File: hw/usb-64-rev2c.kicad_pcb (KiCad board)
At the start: 4 copper layers, 69.2 x 46.5 mm, 64 parts, among them J1 USB_C_Receptacle_PowerOnly_6P, J100 Conn_01x03_Pin, J2 USB_C_Receptacle_USB2.0_14P, J3 USB_C_Receptacle_USB2.0_14P, J300 DE9_Receptacle, J301 DE9_Receptacle, SW1 SW_Push, SW2 SW_Push, U100 NCP1117-3.3_SOT223, U200 RP2040, U201 W25Q128JVSIQ, U300 74AHCT1G125, U301 74AHCT1G125, U302 74AHCT1G125, U303 74AHCT1G125, U304 74AHCT1G125, U305 74AHCT1G125, U306 74AHCT1G125, U307 74AHCT1G125, U308 74AHCT1G125, U309 74AHCT1G125, X100 ASE-12MHz

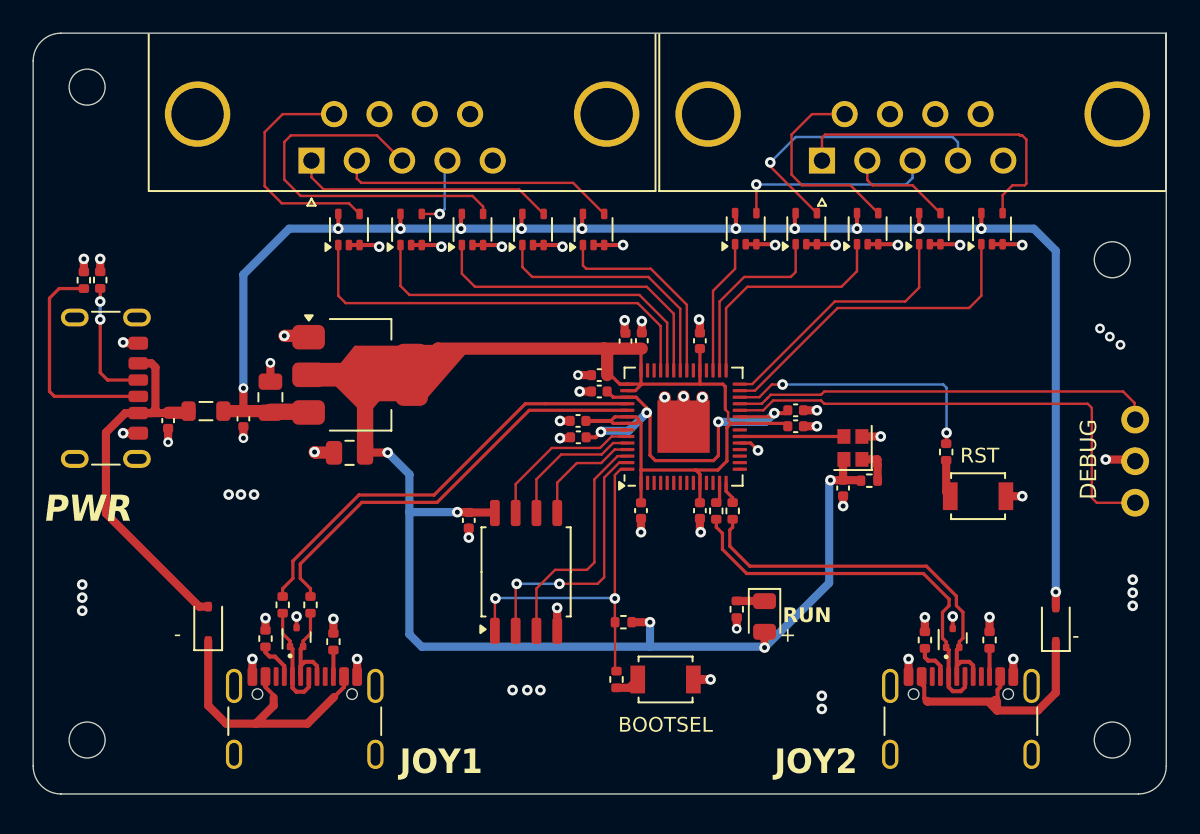
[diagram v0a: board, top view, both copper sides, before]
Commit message: changed pcb specs
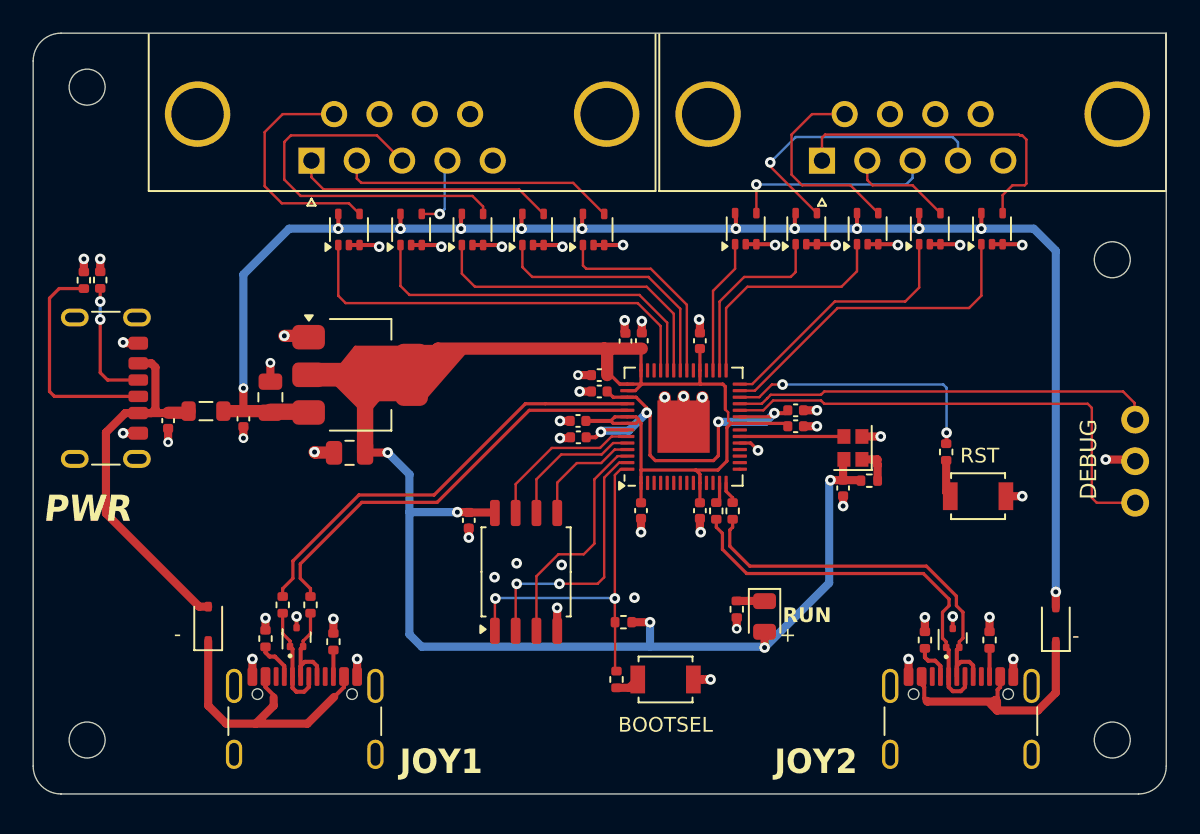
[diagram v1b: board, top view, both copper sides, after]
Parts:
- U100: value NCP1117-3.3_SOT223 -> NCP1117-3.3
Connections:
- J2 pad S1: GND -> unconnected-(J2-SHIELD-PadS1)_1
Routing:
- net GND: vias 69 -> 56
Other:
- board text added: "{ "ViaStitching": "0.2", "stitch_zone_0": { "HSpacing": "2", "VSpacing": "2", "Clearance": "0", "Randomize": false } }"
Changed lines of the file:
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@@
 		(56 "User.7" user)
 		(57 "User.8" user)
-		(58 "User.9" user)
+		(58 "User.9" user "plugins.config")
 	)
 	(setup
@@
 	(net 84 "/MCU/RUN")
 	(net 85 "Net-(R208-Pad2)")
+	(net 86 "unconnected-(J2-SHIELD-PadS1)")
+	(net 87 "unconnected-(J2-SHIELD-PadS1)_1")
+	(net 88 "unconnected-(J2-SHIELD-PadS1)_2")
+	(net 89 "unconnected-(J2-SHIELD-PadS1)_3")
 	(footprint "MountingHole:MountingHole_2.2mm_M2"
 		(layer "F.Cu")
@@
 			)
 		)
-		(property "Value" "NCP1117-3.3_SOT223"
+		(property "Value" "NCP1117-3.3"
 			(at 0 4.5 0)
 			(layer "F.Fab")
@@
 			(layers "*.Cu" "*.Mask" "F.Paste")
 			(remove_unused_layers no)
-			(net 2 "GND")
+			(net 86 "unconnected-(J2-SHIELD-PadS1)")
 			(pinfunction "SHIELD")
-			(pintype "passive")
+			(pintype "passive+no_connect")
 		)
 		(pad "S1" thru_hole oval
@@
 			(layers "*.Cu" "*.Mask" "F.Paste")
 			(remove_unused_layers no)
-			(net 2 "GND")
+			(net 88 "unconnected-(J2-SHIELD-PadS1)_2")
 			(pinfunction "SHIELD")
-			(pintype "passive")
+			(pintype "passive+no_connect")
 		)
 		(pad "S1" thru_hole oval
@@
 			(layers "*.Cu" "*.Mask" "F.Paste")
 			(remove_unused_layers no)
-			(net 2 "GND")
+			(net 89 "unconnected-(J2-SHIELD-PadS1)_3")
 			(pinfunction "SHIELD")
-			(pintype "passive")
+			(pintype "passive+no_connect")
 		)
 		(pad "S1" thru_hole oval
@@
 			(layers "*.Cu" "*.Mask" "F.Paste")
 			(remove_unused_layers no)
-			(net 2 "GND")
+			(net 87 "unconnected-(J2-SHIELD-PadS1)_1")
 			(pinfunction "SHIELD")
-			(pintype "passive")
+			(pintype "passive+no_connect")
 		)
 		(model "${KICAD8_3DMODEL_DIR}/Connector_USB.3dshapes/USB_C_Receptacle_GCT_USB4105-xx-A_16P_TopMnt_Horizontal.wrl"
@@
 		)
 	)
+	(gr_text "{\n  \"ViaStitching\": \"0.2\",\n  \"stitch_zone_0\": {\n    \"HSpacing\": \"2\",\n    \"VSpacing\": \"2\",\n    \"Clearance\": \"0\",\n    \"Randomize\": false\n  }\n}"
+		(at 0 0 0)
+		(layer "User.9")
+		(effects
+			(font
+				(size 1.27 1.27)
+			)
+			(justify left top)
+		)
+	)
 	(segment
 		(start 153.7 86.55)
@@
 	)
 	(via
-		(at 142.3 69.9)
-		(size 0.6)
+		(at 137.2 82.25)
+		(size 0.65)
 		(drill 0.3)
 		(layers "F.Cu" "B.Cu")
@@
 	)
 	(via
-		(at 174.2 67.05)
+		(at 142.3 69.9)
 		(size 0.6)
 		(drill 0.3)
@@
 	)
 	(via
-		(at 140 89.15)
-		(size 0.65)
-		(drill 0.3)
-		(layers "F.Cu" "B.Cu")
-		(free yes)
-		(net 2)
-	)
-	(via
 		(at 141.35 62.05)
 		(size 0.65)
@@
 	)
 	(via
-		(at 157.2 90.3)
-		(size 0.65)
-		(drill 0.3)
-		(layers "F.Cu" "B.Cu")
-		(free yes)
-		(net 2)
-	)
-	(via
 		(at 117.25 74)
 		(size 0.6)
@@
 	)
 	(via
-		(at 121.7 77.2)
-		(size 0.65)
-		(drill 0.3)
-		(layers "F.Cu" "B.Cu")
-		(free yes)
-		(net 2)
-	)
-	(via
 		(at 145.05 61.95)
 		(size 0.65)
@@
 	)
 	(via
-		(at 174.8 67.55)
-		(size 0.6)
-		(drill 0.3)
-		(layers "F.Cu" "B.Cu")
-		(free yes)
-		(net 2)
-	)
-	(via
 		(at 123.2 84.75)
 		(size 0.65)
@@
 	)
 	(via
-		(at 138.3 89.15)
-		(size 0.65)
-		(drill 0.3)
-		(layers "F.Cu" "B.Cu")
-		(free yes)
-		(net 2)
-	)
-	(via
 		(at 121.85 73.75)
 		(size 0.6)
@@
 	)
 	(via
-		(at 139.2 89.15)
+		(at 141.3 81.5)
 		(size 0.65)
 		(drill 0.3)
@@
 	)
 	(via
-		(at 112 83.5)
-		(size 0.65)
-		(drill 0.3)
-		(layers "F.Cu" "B.Cu")
-		(free yes)
-		(net 2)
-	)
-	(via
-		(at 176.2 84)
-		(size 0.65)
-		(drill 0.3)
-		(layers "F.Cu" "B.Cu")
-		(free yes)
-		(net 2)
-	)
-	(via
 		(at 125.1 84.65)
 		(size 0.65)
@@
 	)
 	(via
-		(at 122.5 77.2)
-		(size 0.65)
-		(drill 0.3)
-		(layers "F.Cu" "B.Cu")
-		(free yes)
-		(net 2)
-	)
-	(via
-		(at 176.2 83.2)
-		(size 0.65)
-		(drill 0.3)
-		(layers "F.Cu" "B.Cu")
-		(free yes)
-		(net 2)
-	)
-	(via
 		(at 123.5 69.15)
 		(size 0.6)
@@
 	)
 	(via
-		(at 175.45 68.05)
-		(size 0.6)
+		(at 138.55 81.4)
+		(size 0.65)
 		(drill 0.3)
 		(layers "F.Cu" "B.Cu")
@@
 	)
 	(via
-		(at 157.2 89.5)
-		(size 0.65)
-		(drill 0.3)
-		(layers "F.Cu" "B.Cu")
-		(free yes)
-		(net 2)
-	)
-	(via
 		(at 165.2 84.65)
 		(size 0.65)
@@
 	)
 	(via
-		(at 112 82.7)
-		(size 0.65)
-		(drill 0.3)
-		(layers "F.Cu" "B.Cu")
-		(free yes)
-		(net 2)
-	)
-	(via
-		(at 112 84.3)
-		(size 0.65)
-		(drill 0.3)
-		(layers "F.Cu" "B.Cu")
-		(free yes)
-		(net 2)
-	)
-	(via
-		(at 120.95 77.2)
+		(at 145.75 83.5)
 		(size 0.65)
 		(drill 0.3)
@@
 		(net 2)
 	)
-	(via
-		(at 176.2 82.4)
-		(size 0.65)
-		(drill 0.3)
-		(layers "F.Cu" "B.Cu")
-		(free yes)
-		(net 2)
-	)
 	(segment
 		(start 158.55 73.65)
@@
 	)
 	(segment
-		(start 144.71902 74.85)
-		(end 143.3 76.26902)
+		(start 141.1 80.85)
+		(end 139.76 82.19)
 		(width 0.15)
 		(layer "F.Cu")
@@
 	)
 	(segment
-		(start 139.76 82.94)
-		(end 139.76 85.525)
+		(start 144.71902 74.85)
+		(end 143.3 76.26902)
 		(width 0.15)
 		(layer "F.Cu")
@@
 	)
 	(segment
-		(start 140.9 81.8)
-		(end 139.76 82.94)
+		(start 143.3 76.26902)
+		(end 143.3 80.2)
 		(width 0.15)
 		(layer "F.Cu")
@@
 	)
 	(segment
-		(start 143.3 76.26902)
-		(end 143.3 81.35)
+		(start 145.3125 74.85)
+		(end 144.71902 74.85)
 		(width 0.15)
 		(layer "F.Cu")
@@
 	)
 	(segment
-		(start 145.3125 74.85)
-		(end 144.71902 74.85)
+		(start 142.65 80.85)
+		(end 141.1 80.85)
 		(width 0.15)
 		(layer "F.Cu")
@@
 	)
 	(segment
-		(start 143.3 81.35)
-		(end 142.85 81.8)
+		(start 143.3 80.2)
+		(end 142.65 80.85)
 		(width 0.15)
 		(layer "F.Cu")
@@
 	)
 	(segment
-		(start 142.85 81.8)
-		(end 140.9 81.8)
+		(start 139.76 82.19)
+		(end 139.76 85.525)
 		(width 0.15)
 		(layer "F.Cu")
@@
 	)
 	(via
-		(at 155.55 60.95)
+		(at 127.65 60.95)
 		(size 0.65)
 		(drill 0.3)
@@
 	)
 	(via
-		(at 151.95 60.95)
+		(at 155.55 60.95)
 		(size 0.65)
 		(drill 0.3)
@@
 	)
 	(via
-		(at 127.65 60.95)
+		(at 151.95 60.95)
 		(size 0.65)
 		(drill 0.3)
@@
 		(net_name "GND")
 		(layer "In1.Cu")
+		(name "stitch_zone_0")
 		(hatch edge 0.5)
 		(connect_pads

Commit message: rerouted
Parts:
- C5, C6: footprint Capacitor_SMD:C_0402_1005Metric -> Capacitor_SMD:C_0603_1608Metric
- moved H4 62.9 mm to (119.7, 62.1)
- moved H3 62.4 mm to (174.6, 89.0)
- moved H1 37.2 mm to (119.7, 88.8)
- moved D1 20.1 mm to (165.2, 68.1)
- moved R1 20.0 mm to (163.3, 67.7)
- moved R7 14.3 mm to (125.5, 69.1), turned to 0 degrees
- moved R8 13.0 mm to (125.5, 68.1), turned to 0 degrees
- moved C5 8.26 mm to (125.5, 73.0)
- moved FB3 7.10 mm to (126.5, 70.6)
- moved C100 6.96 mm to (130.5, 71.2)
- moved U100 6.96 mm to (135.9, 69.9)
- moved J1 6.95 mm to (119.3, 70.7)
- moved C101 6.95 mm to (135.3, 74.7)
- moved R203 6.31 mm to (148.5, 83.5)
- moved SW1 5.96 mm to (151.5, 84.0)
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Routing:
- net VBUS: track 120.3 -> 161.6 mm, vias 12 -> 14
- net /C64_controls/JOY1_LEFT: track 23.6 -> 13.8 mm
- net Net-(J1-CC2): track 13.6 -> 4.02 mm
- net /C64_controls/JOY2_RIGHT: track 17.6 -> 10.5 mm
- net /MCU/RUN: track 16.5 -> 11.4 mm
- net USB_DEV_D_N: track 26.1 -> 21.2 mm
- net USB_DEV_D_P: track 25.9 -> 21.2 mm
- net IO2_UP: track 20.3 -> 15.8 mm
- net IO2_FIRE: track 14.4 -> 9.92 mm
- net GND: track 60.7 -> 64.7 mm
- net IO2_DOWN: track 16.1 -> 12.2 mm
- net Net-(J1-CC1): track 7.66 -> 4.17 mm, vias 2 -> 0
- net /MCU/SWCLK: track 30.2 -> 27.1 mm
- net IO2_RIGHT: track 11.3 -> 8.53 mm
- net +3.3V: track 124.4 -> 127.1 mm, vias 5 -> 6
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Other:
- board size 69.2 x 46.5 mm -> 62.2 x 43.2 mm

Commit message: rerouted
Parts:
- added C300: 100n, Capacitor_SMD:C_0402_1005Metric, F.Cu at (137.8, 61.4)
- added C301: 100n, Capacitor_SMD:C_0402_1005Metric, F.Cu at (145.2, 61.4)
- added C302: 100n, Capacitor_SMD:C_0402_1005Metric, F.Cu at (134.0, 61.4)
- added C303: 100n, Capacitor_SMD:C_0402_1005Metric, F.Cu at (130.2, 61.3)
- added C304: 100n, Capacitor_SMD:C_0402_1005Metric, F.Cu at (126.4, 61.4)
- added C305: 100n, Capacitor_SMD:C_0402_1005Metric, F.Cu at (165.8, 61.4)
- added C306: 100n, Capacitor_SMD:C_0402_1005Metric, F.Cu at (162.1, 61.4)
- added C307: 100n, Capacitor_SMD:C_0402_1005Metric, F.Cu at (150.7, 61.3)
- added C308: 100n, Capacitor_SMD:C_0402_1005Metric, F.Cu at (154.4, 61.4)
- added C309: 100n, Capacitor_SMD:C_0402_1005Metric, F.Cu at (158.2, 61.4)
- moved U305 0.15 mm to (167.8, 61.0)
- moved U309 0.15 mm to (160.2, 61.0)
- moved U300 0.15 mm to (139.7, 61.0)
- moved U306 0.15 mm to (163.9, 61.0)
- moved U308 0.10 mm to (156.3, 61.0)
- moved U302 0.05 mm to (135.9, 61.0)
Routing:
- net VBUS: track 161.6 -> 193.1 mm, vias 14 -> 15
- net GND: track 64.7 -> 71.8 mm, vias 56 -> 66
- net +3.3V: track 127.1 -> 121.6 mm, vias 6 -> 7
- net +1V1: track 25.8 -> 28.2 mm
- net IO2_UP: track 15.8 -> 17.4 mm

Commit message: pre production
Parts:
- added ?: , clipboard:7c1455c2-a98c-4e40-9696-5f6f5e7dbb40, F.Cu at (174.2, 77.8)
- moved C211 1.12 mm to (160.2, 77.3)
- moved R207 1.12 mm to (161.8, 76.9)
- moved X100 1.12 mm to (160.8, 74.9)
- moved C204 0.05 mm to (148.8, 78.1)
- moved C205 0.05 mm to (152.4, 78.1)
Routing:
- net GND: track 71.8 -> 85.3 mm, vias 66 -> 170
- net +1V1: track 28.2 -> 24.8 mm, vias 4 -> 3
- net /MCU/MCU_QSPI_SS: track 23.0 -> 19.7 mm, vias 0 -> 2
- net VBUS: track 193.1 -> 191.4 mm, vias 15 -> 13
- net Net-(U200-XIN): track 6.36 -> 5.65 mm
- net +3.3V: track 121.6 -> 121.7 mm, vias 7 -> 5
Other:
- board text added: "BOOT"
- board text removed: "BOOTSEL"
- board text removed: "RUN"
- board text removed: "{ "ViaStitching": "0.2", "stitch_zone_0": { "HSpacing": "2", "VSpacing": "2", "Clearance": "0", "Randomize": false } }"

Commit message: 1p version
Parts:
- removed ?: , clipboard:7c1455c2-a98c-4e40-9696-5f6f5e7dbb40
- removed C100, C101: 10u, Capacitor_SMD:C_0805_2012Metric
- removed C305, C306, C307, C308, C309: 100n, Capacitor_SMD:C_0402_1005Metric
- removed D3: ESD7L5.0DT5G, Package_TO_SOT_SMD:SOT-723
- removed D4, D5: 40V 600mV@1A 1A, Diode_SMD:D_SOD-323
- removed H1, H2, H3, H4: MountingHole, MountingHole:MountingHole_2.2mm_M2
- removed J3: USB_C_Receptacle_USB2.0_14P, Connector_USB:USB_C_Receptacle_GCT_USB4105-xx-A_16P_TopMnt_Horizontal
- removed J301: DE9_Receptacle, Connector_Dsub:DSUB-9_Female_Horizontal_P2.77x2.84mm_EdgePinOffset4.94mm_Housed_MountingHolesOffset4.94mm
- removed R1, R208: 1k, Resistor_SMD:R_0402_1005Metric
- removed R2, R3, R4, R5: 5K1, Resistor_SMD:R_0402_1005Metric
- removed R205, R206: 27R, Resistor_SMD:R_0402_1005Metric
- removed SW2: SW_Push, Button_Switch_SMD:SW_SPST_B3U-1000P
- removed U100: NCP1117-3.3, Package_TO_SOT_SMD:SOT-223-3_TabPin2
- removed U305, U306, U307, U308, U309: 74AHCT1G125, Package_TO_SOT_SMD:SOT-353_SC-70-5
- added C3: 4.7u, Capacitor_SMD:C_1206_3216Metric, F.Cu at (150.9, 86.1)
- added C4: 4.7u, Capacitor_SMD:C_1206_3216Metric, F.Cu at (144.1, 86.1)
- added D6: RED, LED_SMD:LED_0603_1608Metric, F.Cu at (142.4, 90.0)
- added D7: RED, LED_SMD:LED_0603_1608Metric, F.Cu at (141.5, 80.1)
- added IC1: NCP708MU330TAG, Package_SON:SON95P300X300X55-7N, F.Cu at (147.5, 86.4)
- added R6: 330, Resistor_SMD:R_0402_1005Metric, F.Cu at (142.4, 92.5)
- added R9: 330, Resistor_SMD:R_0402_1005Metric, F.Cu at (140.7, 81.8)
- D1: value GREEN -> ESD7L5.0DT5G; footprint LED_SMD:LED_0805_2012Metric -> Package_TO_SOT_SMD:SOT-723
- D2: value ESD7L5.0DT5G -> D_Schottky; footprint Package_TO_SOT_SMD:SOT-723 -> Diode_SMD:D_SOD-323
- J100: value Conn_01x03_Pin -> Conn_01x05_Pin; footprint Connector_PinHeader_2.54mm:PinHeader_1x03_P2.54mm_Vertical -> Connector_PinHeader_2.54mm:PinHeader_1x05_P2.54mm_Vertical
- J2: value USB_C_Receptacle_USB2.0_14P -> USB_A; footprint Connector_USB:USB_C_Receptacle_GCT_USB4105-xx-A_16P_TopMnt_Horizontal -> Connector_USB:CONN_UJ2-AH-SMT_CUD; moved to B.Cu
- J300: footprint Connector_Dsub:DSUB-9_Female_Horizontal_P2.77x2.84mm_EdgePinOffset4.94mm_Housed_MountingHolesOffset4.94mm -> Connector_Dsub:DSUB-9_Female_EdgeMount_P2.77mm
- U201: value W25Q128JVSIQ -> W25Q16JVUXIQ; footprint Package_SO:SOIC-8_5.23x5.23mm_P1.27mm -> Package_SON:Winbond_USON-8-1EP_3x2mm_P0.5mm_EP0.2x1.6mm
- moved R7 39.3 mm to (156.7, 92.9), turned to -90 degrees
- moved J1 38.5 mm to (150.7, 93.0), turned to 0 degrees
- moved J100 35.3 mm to (141.3, 77.5), turned to 180 degrees
- moved C1 32.8 mm to (155.4, 86.6), turned to 0 degrees
- moved D2 31.3 mm to (159.0, 85.5), turned to 180 degrees
- moved R8 31.3 mm to (144.6, 92.9), turned to -90 degrees
- moved U304 30.5 mm to (158.8, 61.9)
- moved FB3 30.4 mm to (153.0, 85.6), turned to 90 degrees
- moved C2 30.2 mm to (155.4, 84.5), turned to 0 degrees
- moved C303 26.7 mm to (156.8, 61.2)
- moved J300 24.9 mm to (150.9, 56.9)
- moved U303 22.8 mm to (154.9, 61.9)
- moved R201 22.3 mm to (149.2, 81.6), turned to -90 degrees
- moved R200 21.7 mm to (150.3, 81.6), turned to -90 degrees
- moved C214 19.9 mm to (160.7, 80.3), turned to 180 degrees
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- renumbered C5 to C1, C6 to C2
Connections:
- C1 pad 1: VBUS -> Net-(C1-Pad1)
- D1 pad 1: Net-(D1-K) -> /USB_MCU_D_P
- D1 pad 2: +3.3V -> /USB_MCU_D_N
- D2 pad 1: USB_MCU_D_N -> Net-(D2-K)
- D2 pad 2: USB_MCU_D_P -> VBUS
- FB3 pad 1: VBUS -> Net-(C1-Pad1)
- J1 pad A9: VBUS -> Net-(C1-Pad1)
- J1 pad B9: VBUS -> Net-(C1-Pad1)
- J100 pad 1: /MCU/SWD -> /MCU/UART_RX
- J100 pad 2: GND -> /MCU/UART_TX
- J100 pad 3: /MCU/SWCLK -> /MCU/SWD
- R200 pad 1: USB_MCU_D_P -> /USB_MCU_D_P
- R200 pad 2: USB_MCU_D_P -> /USB_MCU_D_P
- R201 pad 1: USB_MCU_D_N -> /USB_MCU_D_N
- R201 pad 2: USB_MCU_D_N -> /USB_MCU_D_N
- U200 pad 12: unconnected-(U200-GPIO9-Pad12) -> /C64_controls/IO_FIRE
- U200 pad 13: USB_DEV_D_N -> /C64_controls/IO_RIGHT
- U200 pad 14: USB_DEV_D_P -> /C64_controls/IO_LEFT
- U200 pad 26: /MCU/RUN -> +3.3V
- U200 pad 27: IO2_UP -> /MCU/UART_TX
- U200 pad 28: IO2_DOWN -> /MCU/UART_RX
- U200 pad 29: IO2_FIRE -> unconnected-(U200-GPIO18-Pad29)
- U200 pad 30: IO2_RIGHT -> /C64_controls/IO_DOWN
- U200 pad 31: IO2_LEFT -> /C64_controls/IO_UP
- U200 pad 35: IO_DOWN -> unconnected-(U200-GPIO23-Pad35)
- U200 pad 36: IO_UP -> unconnected-(U200-GPIO24-Pad36)
- U200 pad 37: IO_LEFT -> /MCU/GPIO25
- U200 pad 38: IO_RIGHT -> unconnected-(U200-GPIO26_ADC0-Pad38)
- U200 pad 39: IO_FIRE -> unconnected-(U200-GPIO27_ADC1-Pad39)
- U200 pad 46: USB_MCU_D_N -> /USB_MCU_D_N
- U200 pad 47: USB_MCU_D_P -> /USB_MCU_D_P
- U300 pad 1: IO_UP -> /C64_controls/IO_UP
- U301 pad 1: IO_DOWN -> /C64_controls/IO_DOWN
- U302 pad 1: IO_LEFT -> /C64_controls/IO_LEFT
- U303 pad 1: IO_RIGHT -> /C64_controls/IO_RIGHT
- U304 pad 1: IO_FIRE -> /C64_controls/IO_FIRE
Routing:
- net VBUS: track 191.4 -> 76.4 mm, vias 13 -> 6
- net USB_MCU_D_N: track 31.9 -> 0.00 mm
- net USB_MCU_D_P: track 31.2 -> 0.00 mm
- net GND: track 85.3 -> 54.2 mm, vias 170 -> 82
- net IO_FIRE: track 27.6 -> 0.00 mm
- net /USB_MCU_D_P: track 0.00 -> 25.6 mm, vias 0 -> 1
- net /USB_MCU_D_N: track 0.00 -> 25.3 mm, vias 0 -> 1
- net IO_RIGHT: track 24.6 -> 0.00 mm
- net USB_DEV_D_P: track 21.2 -> 0.00 mm
- net USB_DEV_D_N: track 21.2 -> 0.00 mm
- net IO_LEFT: track 21.0 -> 0.00 mm
- net /C64_controls/JOY2_UP: track 19.1 -> 0.00 mm
- net +3.3V: track 121.7 -> 102.6 mm, vias 5 -> 4
- net IO_UP: track 18.1 -> 0.00 mm
- net IO2_UP: track 17.4 -> 0.00 mm
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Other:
- board size 62.2 x 43.2 mm -> 24.5 x 41 mm
- board text added: "CLK"
- board text added: "CS"
- board text added: "D"
- board text added: "G"
- board text added: "LLIC64"
- board text added: "RX"
- board text added: "Rev. 2c"
- board text added: "TX"
- board text added: "github.com/marcopiovanello"
- board text removed: "+"
- board text removed: "-"
- board text removed: "BOOT"
- board text removed: "Control port USB converter"
- board text removed: "DEBUG"
- board text removed: "JOY1"
- board text removed: "JOY2"
- board text removed: "RST"
- board text removed: "USB64"
- board text removed: "github.com/marcopiovanello/usb64"

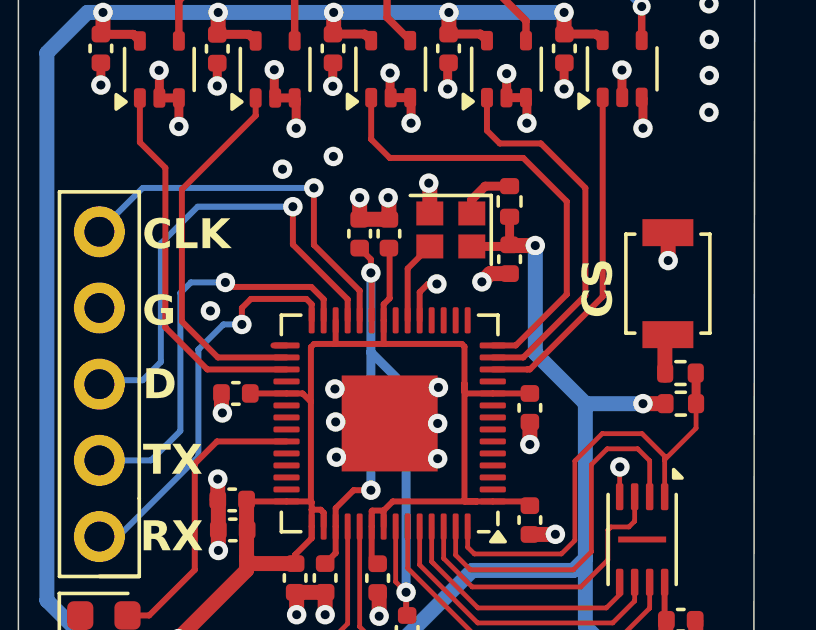
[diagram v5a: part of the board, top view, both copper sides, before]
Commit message: added 15pf load capacitor for oscillator
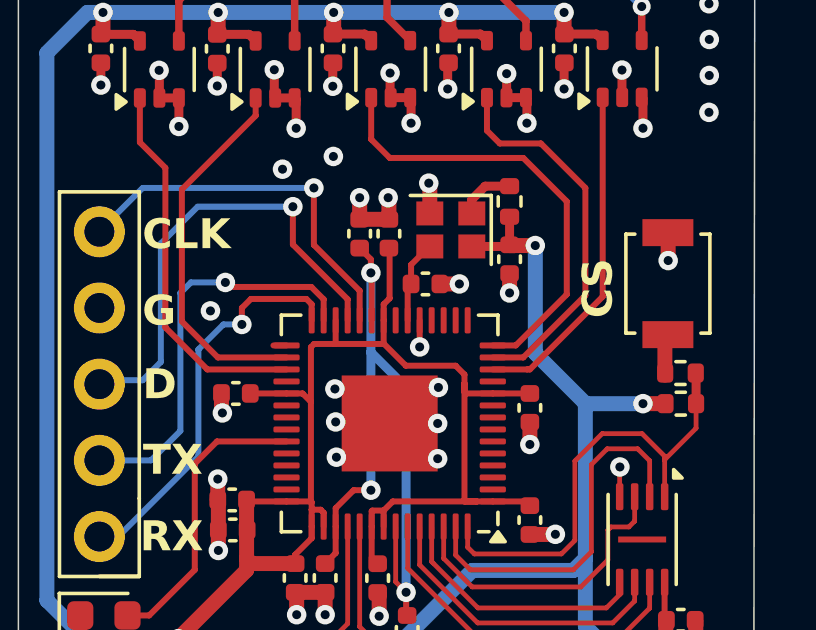
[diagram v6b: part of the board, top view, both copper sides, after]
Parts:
- added C215: 15p, Capacitor_SMD:C_0402_1005Metric, F.Cu at (152.2, 69.0)
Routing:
- net +3.3V: track 102.6 -> 102.1 mm
- net GND: track 54.2 -> 53.8 mm, vias 82 -> 83
